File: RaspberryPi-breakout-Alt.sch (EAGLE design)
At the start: 3 parts

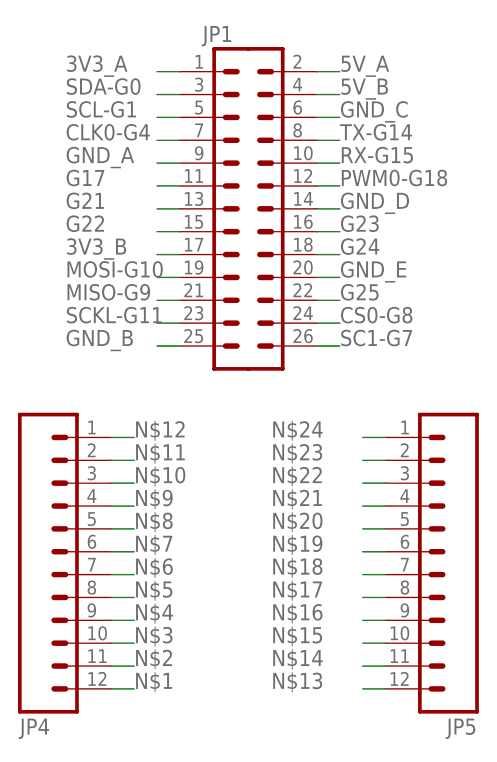
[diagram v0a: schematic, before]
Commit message: Fleshed out some of the pins
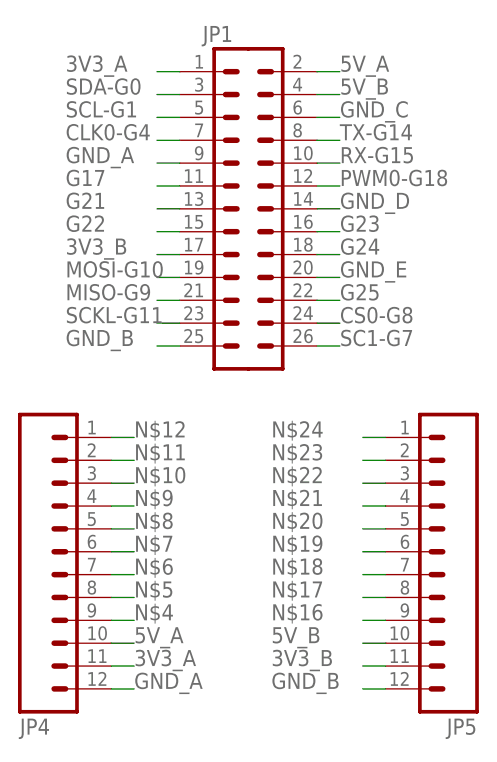
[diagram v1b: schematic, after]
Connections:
- removed net N$1: JP4.12
- removed net N$13: JP5.12
- removed net N$14: JP5.11
- removed net N$15: JP5.10
- removed net N$2: JP4.11
- removed net N$3: JP4.10
- net 3V3_A: now also JP4.11
- net 3V3_B: now also JP5.11
- net 5V_A: now also JP4.10
- net 5V_B: now also JP5.10
- net GND_A: now also JP4.12
- net GND_B: now also JP5.12
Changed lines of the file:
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@@
 <label x="5.08" y="71.12" size="1.778" layer="95"/>
+</segment>
+<segment>
+<pinref part="JP4" gate="G$1" pin="11"/>
+<wire x1="10.16" y1="5.08" x2="12.7" y2="5.08" width="0.1524" layer="91"/>
+<label x="12.7" y="5.08" size="1.778" layer="95"/>
 </segment>
 </net>
@@
 <label x="5.08" y="60.96" size="1.778" layer="95"/>
 </segment>
+<segment>
+<pinref part="JP4" gate="G$1" pin="12"/>
+<wire x1="10.16" y1="2.54" x2="12.7" y2="2.54" width="0.1524" layer="91"/>
+<label x="12.7" y="2.54" size="1.778" layer="95"/>
+</segment>
 </net>
 <net name="G17" class="0">
@@
 <label x="5.08" y="50.8" size="1.778" layer="95"/>
 </segment>
+<segment>
+<pinref part="JP5" gate="G$1" pin="11"/>
+<wire x1="40.64" y1="5.08" x2="38.1" y2="5.08" width="0.1524" layer="91"/>
+<label x="27.94" y="5.08" size="1.778" layer="95"/>
+</segment>
 </net>
 <net name="MOSI-G10" class="0">
@@
 <label x="5.08" y="40.64" size="1.778" layer="95"/>
 </segment>
+<segment>
+<pinref part="JP5" gate="G$1" pin="12"/>
+<wire x1="40.64" y1="2.54" x2="38.1" y2="2.54" width="0.1524" layer="91"/>
+<label x="27.94" y="2.54" size="1.778" layer="95"/>
+</segment>
 </net>
 <net name="SC1-G7" class="0">
@@
 <label x="35.56" y="68.58" size="1.778" layer="95"/>
 </segment>
+<segment>
+<pinref part="JP5" gate="G$1" pin="10"/>
+<wire x1="40.64" y1="7.62" x2="38.1" y2="7.62" width="0.1524" layer="91"/>
+<label x="27.94" y="7.62" size="1.778" layer="95"/>
+</segment>
 </net>
 <net name="5V_A" class="0">
@@
 <label x="35.56" y="71.12" size="1.778" layer="95"/>
 </segment>
-</net>
-<net name="N$1" class="0">
-<segment>
-<pinref part="JP4" gate="G$1" pin="12"/>
-<wire x1="10.16" y1="2.54" x2="12.7" y2="2.54" width="0.1524" layer="91"/>
-<label x="12.7" y="2.54" size="1.778" layer="95"/>
-</segment>
-</net>
-<net name="N$2" class="0">
-<segment>
-<pinref part="JP4" gate="G$1" pin="11"/>
-<wire x1="10.16" y1="5.08" x2="12.7" y2="5.08" width="0.1524" layer="91"/>
-<label x="12.7" y="5.08" size="1.778" layer="95"/>
-</segment>
-</net>
-<net name="N$3" class="0">
 <segment>
 <pinref part="JP4" gate="G$1" pin="10"/>
@@
 </segment>
 </net>
-<net name="N$13" class="0">
-<segment>
-<pinref part="JP5" gate="G$1" pin="12"/>
-<wire x1="40.64" y1="2.54" x2="38.1" y2="2.54" width="0.1524" layer="91"/>
-<label x="27.94" y="2.54" size="1.778" layer="95"/>
-</segment>
-</net>
-<net name="N$14" class="0">
-<segment>
-<pinref part="JP5" gate="G$1" pin="11"/>
-<wire x1="40.64" y1="5.08" x2="38.1" y2="5.08" width="0.1524" layer="91"/>
-<label x="27.94" y="5.08" size="1.778" layer="95"/>
-</segment>
-</net>
-<net name="N$15" class="0">
-<segment>
-<pinref part="JP5" gate="G$1" pin="10"/>
-<wire x1="40.64" y1="7.62" x2="38.1" y2="7.62" width="0.1524" layer="91"/>
-<label x="27.94" y="7.62" size="1.778" layer="95"/>
-</segment>
-</net>
